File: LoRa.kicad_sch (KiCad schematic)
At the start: 20 parts, among them IC8 317990687, J6 Conn_Coaxial, Q8 IRLML6402, X6 Conn_01x06_Pin

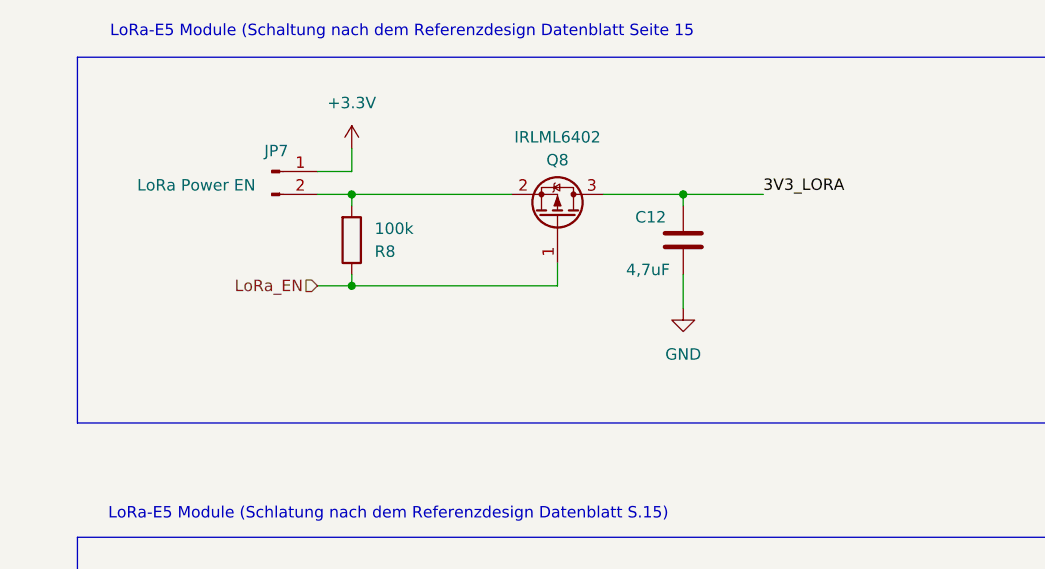
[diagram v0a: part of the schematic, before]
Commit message: Add SamacSys & CAPPRD library; update KiCad
Add a new SamacSys parts library and a complete CAPPRD500 footprint/package set (870585375004) with multi-EDA exports and 3D STEP models. Also add sym-lib-table and SamacSys parts entries, and update KiCad project files (schematics, PCB, project file and generated PDFs) to reference the new parts and footprints.
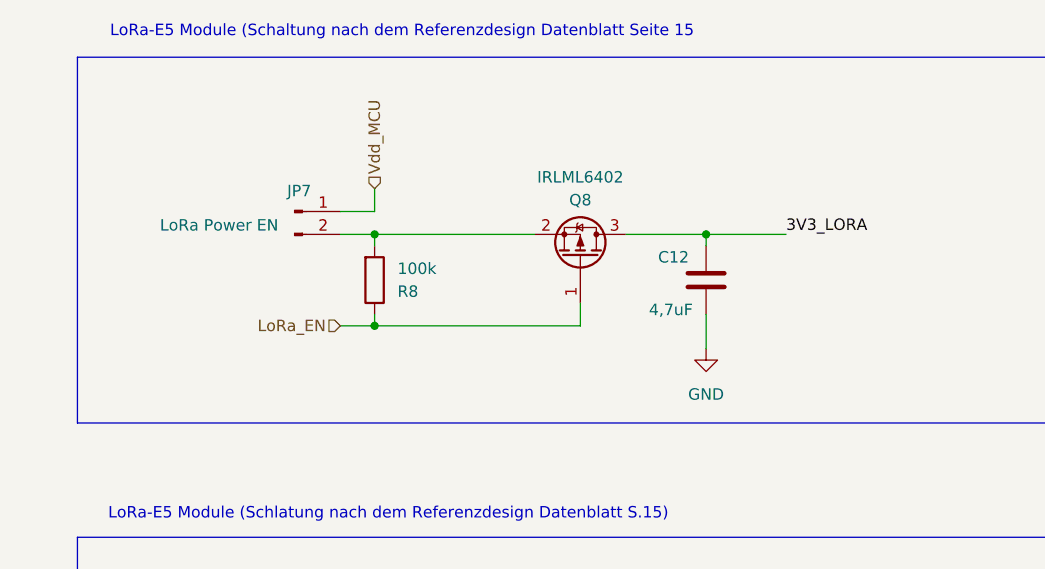
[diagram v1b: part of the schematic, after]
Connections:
- net +3.3V renamed Vdd_MCU
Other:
- moved on the sheet: C12, JP7, Q8, R8
